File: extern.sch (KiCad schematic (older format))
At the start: 1 part, among them J9 Conn_02x03_Odd_Even

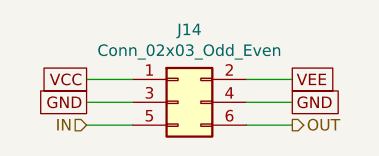
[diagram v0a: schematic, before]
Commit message: inverted LF processing chain, now with BW2 subsonic filter
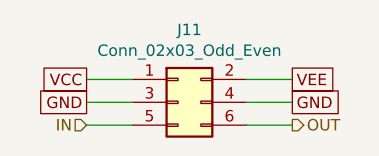
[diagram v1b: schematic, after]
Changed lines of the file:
@@
 $Descr A4 11693 8268
 encoding utf-8
-Sheet 17 19
+Sheet 15 17
 Title "Header for external transform"
 Date "2021-10-05"
@@
 AR Path="/6184255F/6180F76B" Ref="J11"  Part="1"
 AR Path="/618480AF/6180F76B" Ref="J12"  Part="1"
-AR Path="/619F9CA2/6180F76B" Ref="J13"  Part="1"
-AR Path="/61A91437/6180F76B" Ref="J14"  Part="1"
-F 0 "J14" H 4150 2717 50  0000 C CNN
+AR Path="/619F9CA2/6180F76B" Ref="J?"  Part="1"
+AR Path="/61A91437/6180F76B" Ref="J13"  Part="1"
+F 0 "J11" H 4150 2717 50  0000 C CNN
 F 1 "Conn_02x03_Odd_Even" H 4150 2626 50  0000 C CNN
 F 2 "Pin_Headers:Pin_Header_Straight_2x03_Pitch2.54mm" H 4100 2400 50  0001 C CNN

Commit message: Board is placed and about half-routed
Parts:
- renumbered J9 to J10
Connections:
- net VCC: now also J10.2 (Pin_2); no longer J10.1 (Pin_1)
- net VEE: now also J10.1 (Pin_1); no longer J10.2 (Pin_2)
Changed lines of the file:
@@
 $Descr A4 11693 8268
 encoding utf-8
-Sheet 15 17
+Sheet 17 17
 Title "Header for external transform"
 Date "2021-10-05"
@@
 Text HLabel 4600 2500 2    50   Output ~ 0
 OUT
-Text GLabel 3700 2300 0    50   UnSpc ~ 0
+Text GLabel 4600 2300 2    50   UnSpc ~ 0
 VCC
 Text GLabel 3700 2400 0    50   UnSpc ~ 0
 GND
-Text GLabel 4600 2300 2    50   UnSpc ~ 0
+Text GLabel 3700 2300 0    50   UnSpc ~ 0
 VEE
 $Comp
-L Connector_Generic:Conn_02x03_Odd_Even J9
+L Connector_Generic:Conn_02x03_Odd_Even J10
 U 1 1 6180F76B
 P 4100 2400
-AR Path="/6180EB75/6180F76B" Ref="J9"  Part="1"
-AR Path="/618349E5/6180F76B" Ref="J10"  Part="1"
-AR Path="/6184255F/6180F76B" Ref="J11"  Part="1"
-AR Path="/618480AF/6180F76B" Ref="J12"  Part="1"
+AR Path="/6180EB75/6180F76B" Ref="J10"  Part="1"
+AR Path="/618349E5/6180F76B" Ref="J11"  Part="1"
+AR Path="/6184255F/6180F76B" Ref="J12"  Part="1"
+AR Path="/618480AF/6180F76B" Ref="J13"  Part="1"
 AR Path="/619F9CA2/6180F76B" Ref="J?"  Part="1"
-AR Path="/61A91437/6180F76B" Ref="J13"  Part="1"
-F 0 "J11" H 4150 2717 50  0000 C CNN
+AR Path="/61A91437/6180F76B" Ref="J14"  Part="1"
+F 0 "J14" H 4150 2717 50  0000 C CNN
 F 1 "Conn_02x03_Odd_Even" H 4150 2626 50  0000 C CNN
 F 2 "Pin_Headers:Pin_Header_Straight_2x03_Pitch2.54mm" H 4100 2400 50  0001 C CNN
